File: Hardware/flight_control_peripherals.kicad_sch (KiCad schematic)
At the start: 17 parts, among them J10 Conn_02x06_Odd_Even, J11 Conn_01x06, J12 Micro_SD_Card_Det1, J6 Conn_01x10, J7 Conn_02x10_Odd_Even, J8 Conn_01x04, J9 Conn_01x04, U13 W25N01GVZEIG_TR, U14 24CW1280T-I/OT, U15 PCA9685PW_118

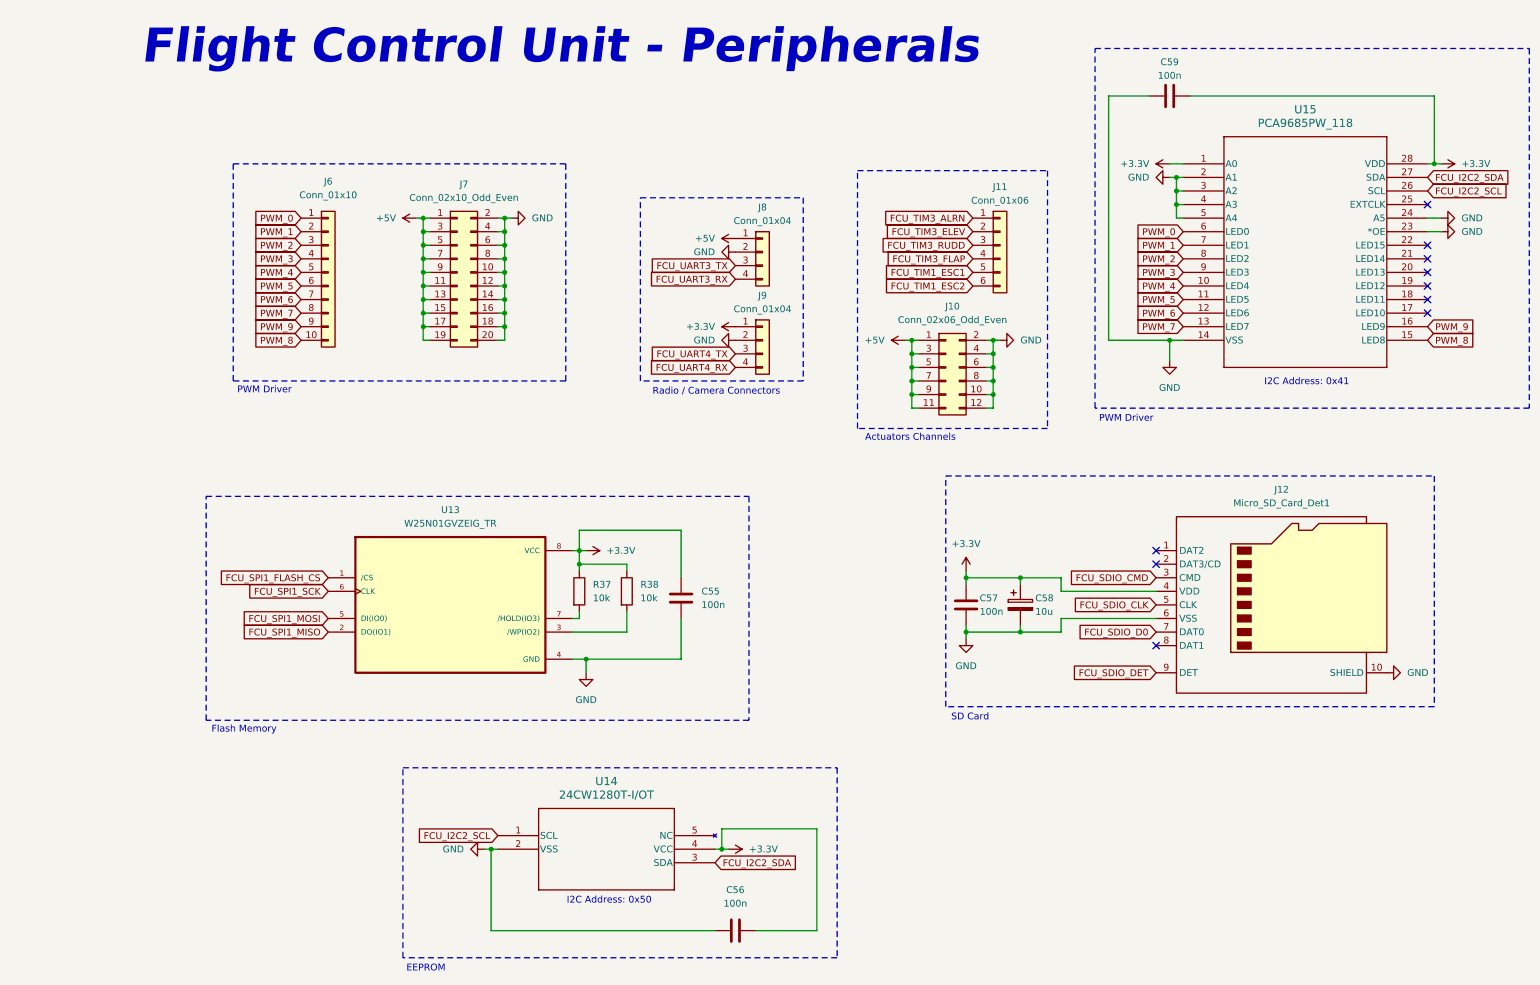
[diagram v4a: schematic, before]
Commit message: version 0.1.1, added dfu usb to firmware upload, changed pwm channels
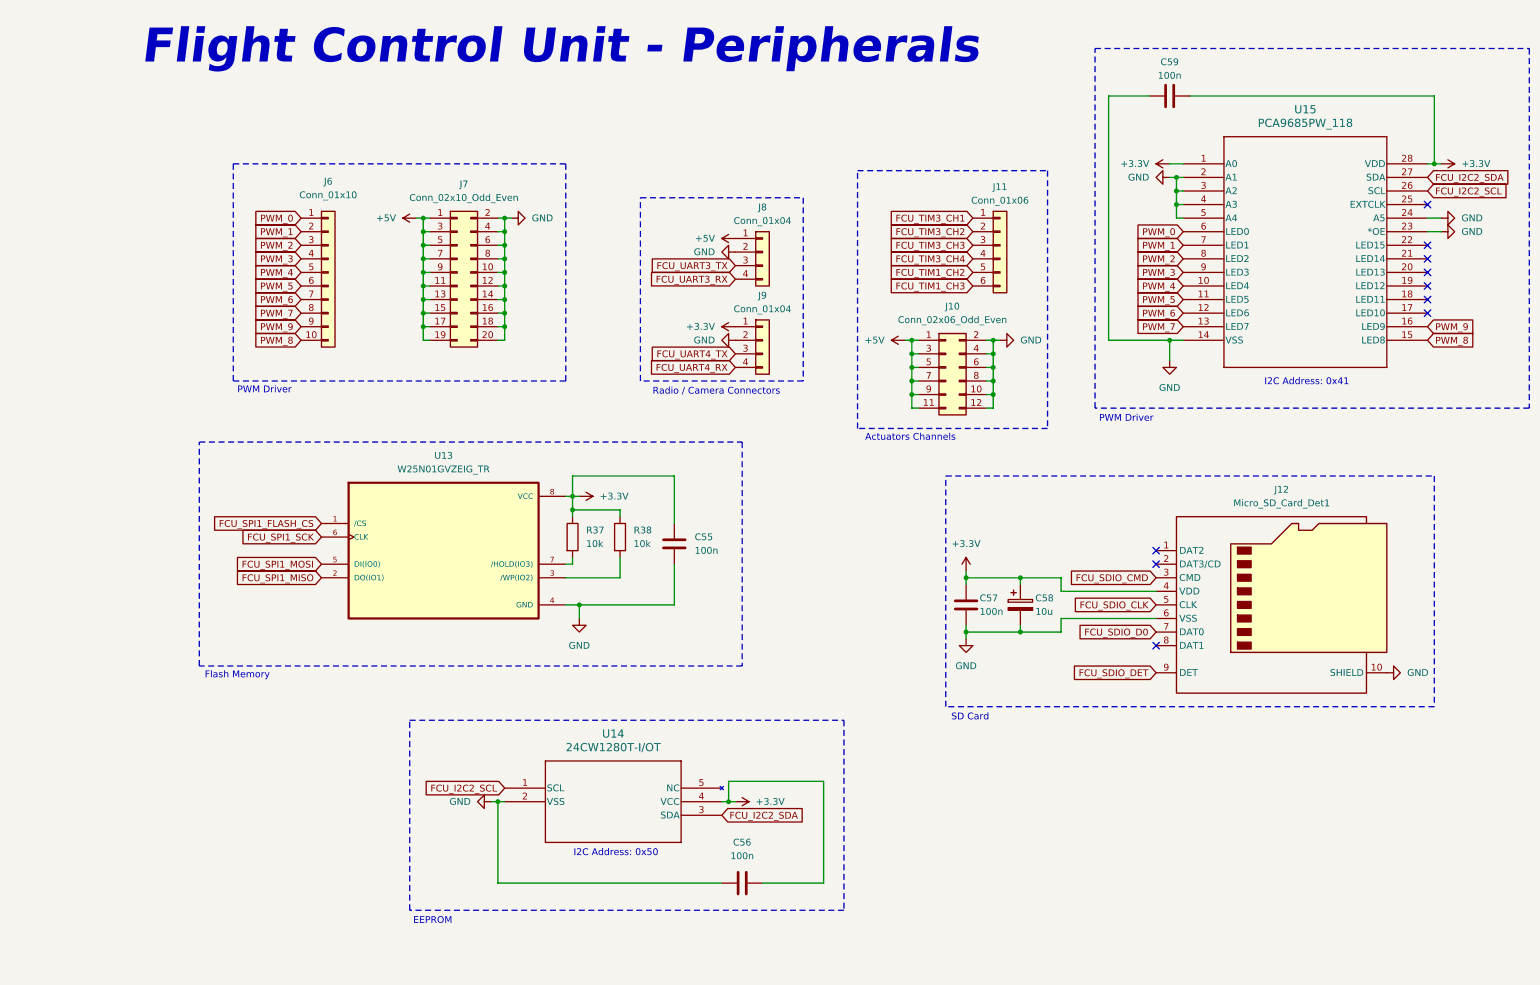
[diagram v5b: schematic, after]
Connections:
- net FCU_TIM1_ESC1 renamed FCU_TIM1_CH2
- net FCU_TIM1_ESC2 renamed FCU_TIM1_CH3
- net FCU_TIM3_ALRN renamed FCU_TIM3_CH1
- net FCU_TIM3_ELEV renamed FCU_TIM3_CH2
- net FCU_TIM3_FLAP renamed FCU_TIM3_CH4
- net FCU_TIM3_RUDD renamed FCU_TIM3_CH3
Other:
- moved on the sheet: C55, C56, R37, R38, U13, U14
